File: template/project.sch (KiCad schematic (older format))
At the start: 1 part

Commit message: Continued play with libraries
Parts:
- added SW1: SW_Push, Buttons_Switches_SMD:SW_SPST_FSMSM, symbol SW_Push
- BT1: renamed from BT?; footprint (none) -> Battery_Holders:Keystone_103_1x20mm-CoinCell
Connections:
- net +3V3: now also SW1.1
- net Sheet59D70135/V_IN renamed reg/V_IN
- new net blue led/IN: SW1.2
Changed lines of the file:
@@
 $Descr A4 11693 8268
 encoding utf-8
-Sheet 1 3
+Sheet 1 5
 Title ""
 Date ""
@@
 S 4350 2800 500  150
 U 59D6FE5B
-F0 "Sheet59D6FE5A" 60
+F0 "green led" 60
 F1 "3v3/led/green.sch" 60
-F2 "3V3" I L 4350 2850 60
+F2 "IN" I L 4350 2850 60
 $EndSheet
 $Comp
-L Battery BT?
+L Battery BT1
 U 1 1 59D6FF4B
 P 3400 3950
-F 0 "BT?" H 3500 4050 50  0000 L CNN
+F 0 "BT1" H 3500 4050 50  0000 L CNN
 F 1 "Battery" H 3500 3950 50  0000 L CNN
-F 2 "" V 3400 4010 50  0001 C CNN
+F 2 "Battery_Holders:Keystone_103_1x20mm-CoinCell" V 3400 4010 50  0001 C CNN
 F 3 "" V 3400 4010 50  0001 C CNN
 	1    3400 3950
@@
 L GND #PWR01
 U 1 1 59D6FFA3
-P 3400 4150
-F 0 "#PWR01" H 3400 3900 50  0001 C CNN
-F 1 "GND" H 3400 4000 50  0000 C CNN
-F 2 "" H 3400 4150 50  0001 C CNN
-F 3 "" H 3400 4150 50  0001 C CNN
-	1    3400 4150
+P 3700 4350
+F 0 "#PWR01" H 3700 4100 50  0001 C CNN
+F 1 "GND" H 3700 4200 50  0000 C CNN
+F 2 "" H 3700 4350 50  0001 C CNN
+F 3 "" H 3700 4350 50  0001 C CNN
+	1    3700 4350
 	1    0    0    -1
 $EndComp
@@
 S 3900 3650 650  200
 U 59D70136
-F0 "Sheet59D70135" 60
+F0 "reg" 60
 F1 "3v3/reg.sch" 60
 F2 "V_IN" I L 3900 3750 60
@@
 Wire Wire Line
 	3400 3750 3900 3750
+Wire Wire Line
+	5100 3750 4550 3750
+Wire Wire Line
+	4000 2850 4350 2850
 $Comp
-L +3V3 #PWR02
+L PWR_FLAG #FLG02
+U 1 1 59D70465
+P 3450 3750
+F 0 "#FLG02" H 3450 3825 50  0001 C CNN
+F 1 "PWR_FLAG" H 3450 3900 50  0000 C CNN
+F 2 "" H 3450 3750 50  0001 C CNN
+F 3 "" H 3450 3750 50  0001 C CNN
+	1    3450 3750
+	1    0    0    -1
+$EndComp
+Connection ~ 3450 3750
+Wire Wire Line
+	3400 4350 3700 4350
+$Comp
+L PWR_FLAG #FLG03
+U 1 1 59D704F4
+P 3700 4350
+F 0 "#FLG03" H 3700 4425 50  0001 C CNN
+F 1 "PWR_FLAG" H 3700 4500 50  0000 C CNN
+F 2 "" H 3700 4350 50  0001 C CNN
+F 3 "" H 3700 4350 50  0001 C CNN
+	1    3700 4350
+	1    0    0    -1
+$EndComp
+Wire Wire Line
+	3400 4150 3400 4350
+$Sheet
+S 4450 2150 500  150
+U 59D70D6B
+F0 "blue led" 60
+F1 "3v3/led/blue.sch" 60
+F2 "IN" I L 4450 2200 60
+$EndSheet
+$Comp
+L SW_Push SW1
+U 1 1 59D70D94
+P 4150 2200
+F 0 "SW1" H 4200 2300 50  0000 L CNN
+F 1 "SW_Push" H 4150 2140 50  0000 C CNN
+F 2 "Buttons_Switches_SMD:SW_SPST_FSMSM" H 4150 2400 50  0001 C CNN
+F 3 "" H 4150 2400 50  0001 C CNN
+	1    4150 2200
+	1    0    0    -1
+$EndComp
+Wire Wire Line
+	4350 2200 4450 2200
+$Comp
+L +3V3 #PWR04
 U 1 1 59D7025D
 P 5100 3750
-F 0 "#PWR02" H 5100 3600 50  0001 C CNN
+F 0 "#PWR04" H 5100 3600 50  0001 C CNN
 F 1 "+3V3" H 5100 3890 50  0000 C CNN
 F 2 "" H 5100 3750 50  0001 C CNN
@@
 	1    0    0    -1
 $EndComp
-Wire Wire Line
-	5100 3750 4550 3750
 $Comp
-L +3V3 #PWR03
+L +3V3 #PWR05
 U 1 1 59D70291
 P 4000 2850
-F 0 "#PWR03" H 4000 2700 50  0001 C CNN
+F 0 "#PWR05" H 4000 2700 50  0001 C CNN
 F 1 "+3V3" H 4000 2990 50  0000 C CNN
 F 2 "" H 4000 2850 50  0001 C CNN
@@
 	1    0    0    -1
 $EndComp
+$Comp
+L +3V3 #PWR06
+U 1 1 59D70DD7
+P 3950 2200
+F 0 "#PWR06" H 3950 2050 50  0001 C CNN
+F 1 "+3V3" H 3950 2340 50  0000 C CNN
+F 2 "" H 3950 2200 50  0001 C CNN
+F 3 "" H 3950 2200 50  0001 C CNN
+	1    3950 2200
+	1    0    0    -1
+$EndComp
+$Sheet
+S 5700 2600 500  150
+U 59D71FBB
+F0 "red led" 60
+F1 "3v3/led/red.sch" 60
+F2 "IN" I L 5700 2650 60
+$EndSheet
 Wire Wire Line
-	4000 2850 4350 2850
+	4200 2850 4200 2600
 Wire Wire Line
-	4350 2850 4350 2850
+	4200 2600 5550 2600
+Wire Wire Line
+	5550 2600 5550 2650
+Wire Wire Line
+	5550 2650 5700 2650
+Connection ~ 4200 2850
 $EndSCHEMATC

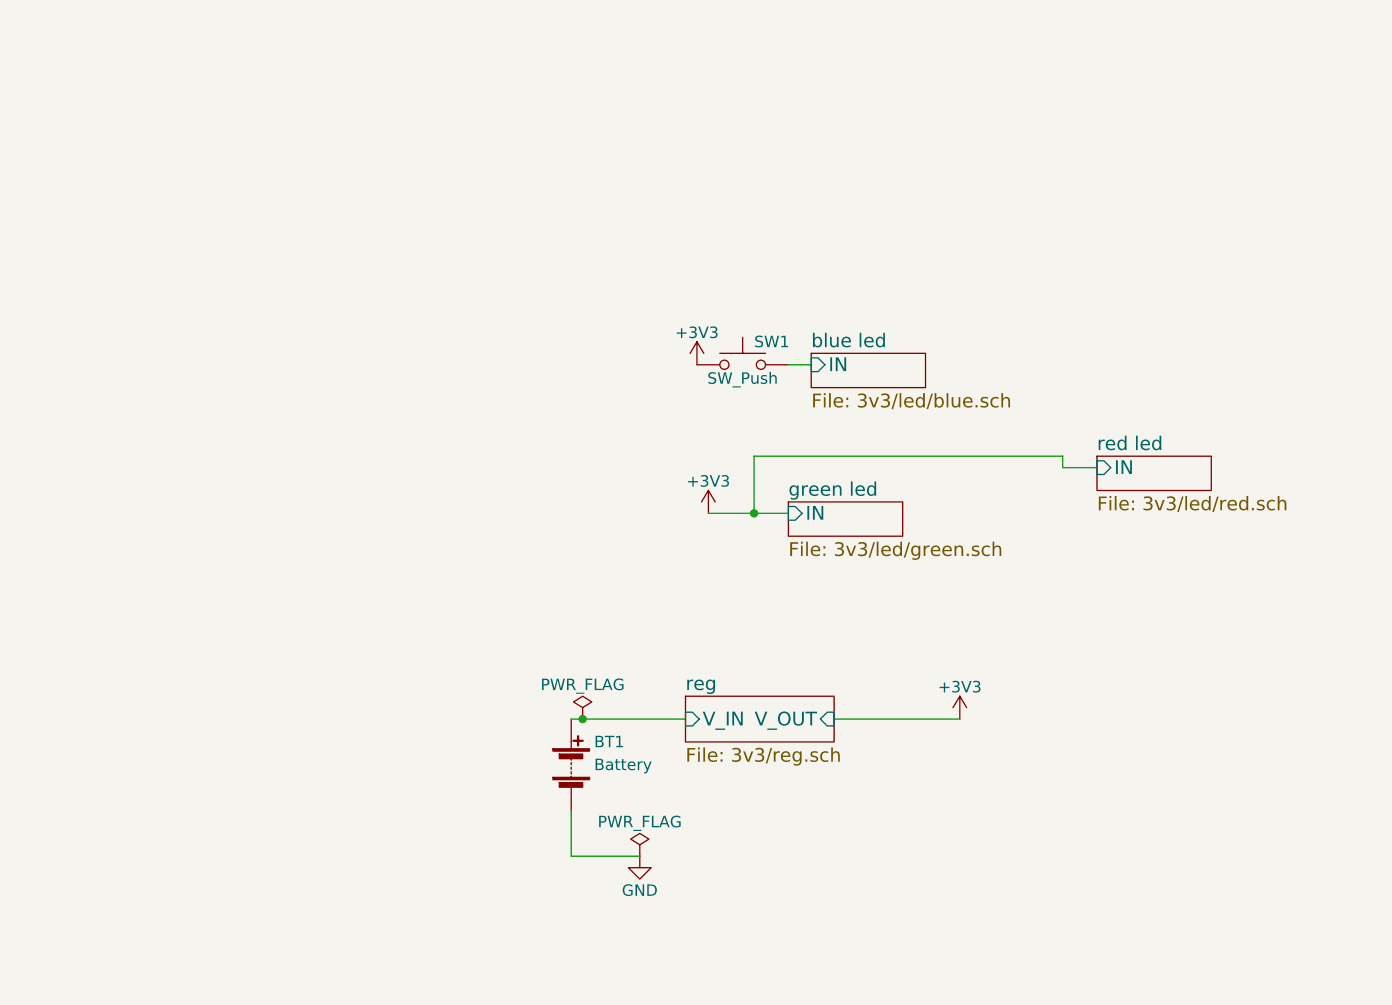
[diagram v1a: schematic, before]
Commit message: Added USB_UART connector
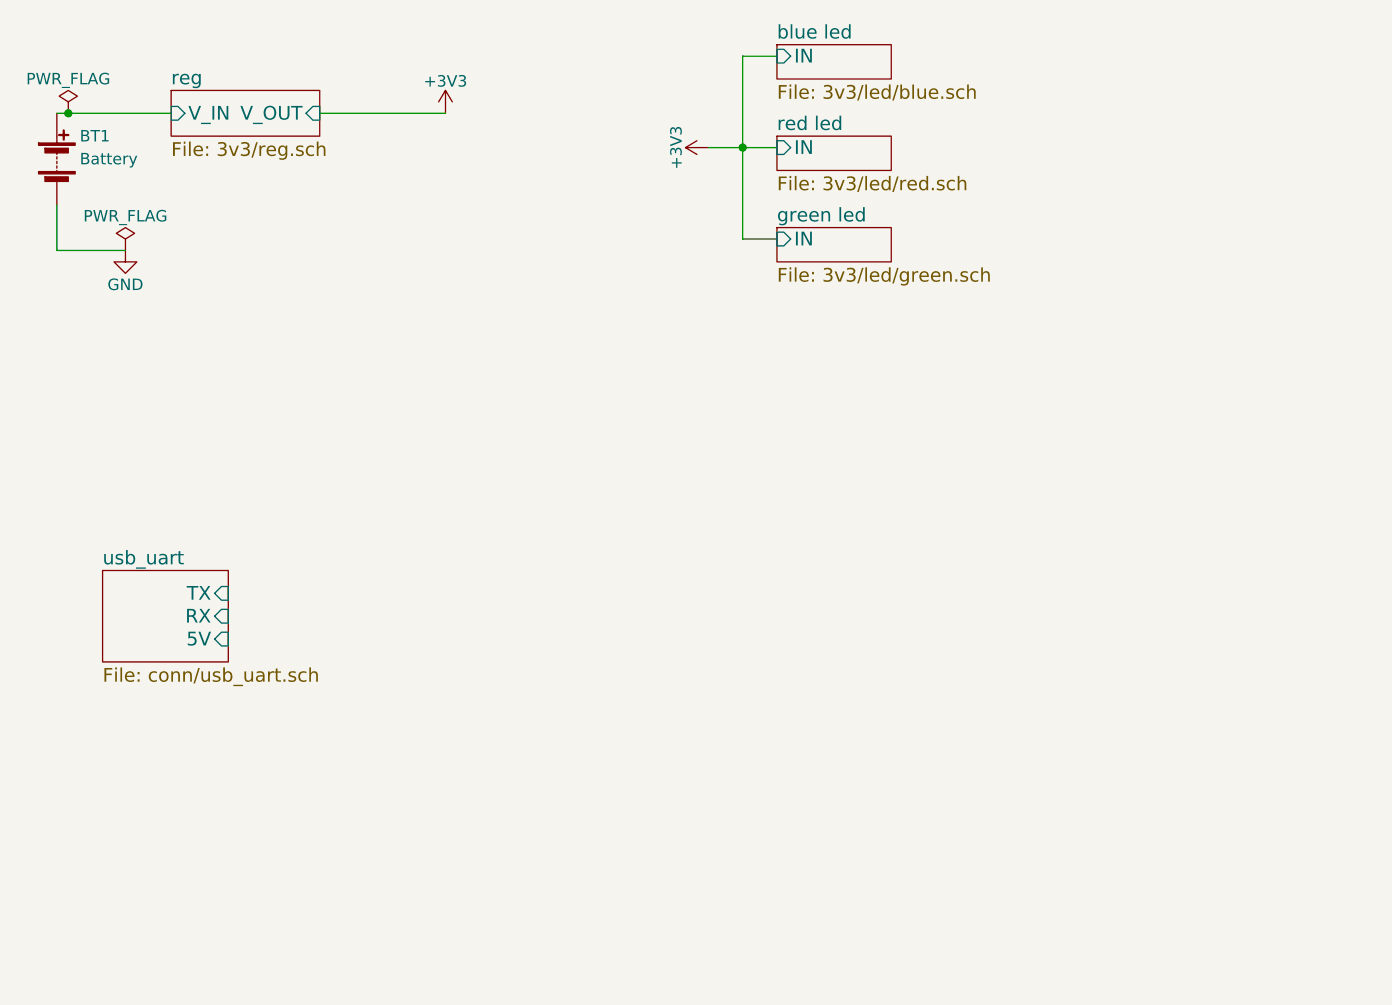
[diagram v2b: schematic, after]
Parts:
- removed SW1: SW_Push, Buttons_Switches_SMD:SW_SPST_FSMSM, symbol SW_Push
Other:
- moved on the sheet: BT1
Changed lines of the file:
@@
 EESchema Schematic File Version 2
+LIBS:ft230xs
+LIBS:usb_microb
 LIBS:power
 LIBS:device
@@
 LIBS:contrib
 LIBS:valves
+LIBS:project-cache
 EELAYER 25 0
 EELAYER END
 $Descr A4 11693 8268
 encoding utf-8
-Sheet 1 5
+Sheet 1 6
 Title ""
 Date ""
@@
 $EndDescr
 $Sheet
-S 4350 2800 500  150
+S 4300 1600 500  150
 U 59D6FE5B
 F0 "green led" 60
 F1 "3v3/led/green.sch" 60
-F2 "IN" I L 4350 2850 60
+F2 "IN" I L 4300 1650 60
 $EndSheet
 $Comp
 L Battery BT1
 U 1 1 59D6FF4B
-P 3400 3950
-F 0 "BT1" H 3500 4050 50  0000 L CNN
-F 1 "Battery" H 3500 3950 50  0000 L CNN
-F 2 "Battery_Holders:Keystone_103_1x20mm-CoinCell" V 3400 4010 50  0001 C CNN
-F 3 "" V 3400 4010 50  0001 C CNN
-	1    3400 3950
+P 1150 1300
+F 0 "BT1" H 1250 1400 50  0000 L CNN
+F 1 "Battery" H 1250 1300 50  0000 L CNN
+F 2 "Battery_Holders:Keystone_103_1x20mm-CoinCell" V 1150 1360 50  0001 C CNN
+F 3 "" V 1150 1360 50  0001 C CNN
+	1    1150 1300
 	1    0    0    -1
 $EndComp
@@
 L GND #PWR01
 U 1 1 59D6FFA3
-P 3700 4350
-F 0 "#PWR01" H 3700 4100 50  0001 C CNN
-F 1 "GND" H 3700 4200 50  0000 C CNN
-F 2 "" H 3700 4350 50  0001 C CNN
-F 3 "" H 3700 4350 50  0001 C CNN
-	1    3700 4350
+P 1450 1700
+F 0 "#PWR01" H 1450 1450 50  0001 C CNN
+F 1 "GND" H 1450 1550 50  0000 C CNN
+F 2 "" H 1450 1700 50  0001 C CNN
+F 3 "" H 1450 1700 50  0001 C CNN
+	1    1450 1700
 	1    0    0    -1
 $EndComp
 $Sheet
-S 3900 3650 650  200
+S 1650 1000 650  200
 U 59D70136
 F0 "reg" 60
 F1 "3v3/reg.sch" 60
-F2 "V_IN" I L 3900 3750 60
-F3 "V_OUT" I R 4550 3750 60
+F2 "V_IN" I L 1650 1100 60
+F3 "V_OUT" I R 2300 1100 60
 $EndSheet
 Wire Wire Line
-	3400 3750 3900 3750
+	1150 1100 1650 1100
 Wire Wire Line
-	5100 3750 4550 3750
-Wire Wire Line
-	4000 2850 4350 2850
+	2850 1100 2300 1100
 $Comp
 L PWR_FLAG #FLG02
 U 1 1 59D70465
-P 3450 3750
-F 0 "#FLG02" H 3450 3825 50  0001 C CNN
-F 1 "PWR_FLAG" H 3450 3900 50  0000 C CNN
-F 2 "" H 3450 3750 50  0001 C CNN
-F 3 "" H 3450 3750 50  0001 C CNN
-	1    3450 3750
+P 1200 1100
+F 0 "#FLG02" H 1200 1175 50  0001 C CNN
+F 1 "PWR_FLAG" H 1200 1250 50  0000 C CNN
+F 2 "" H 1200 1100 50  0001 C CNN
+F 3 "" H 1200 1100 50  0001 C CNN
+	1    1200 1100
 	1    0    0    -1
 $EndComp
-Connection ~ 3450 3750
+Connection ~ 1200 1100
 Wire Wire Line
-	3400 4350 3700 4350
+	1150 1700 1450 1700
 $Comp
 L PWR_FLAG #FLG03
 U 1 1 59D704F4
-P 3700 4350
-F 0 "#FLG03" H 3700 4425 50  0001 C CNN
-F 1 "PWR_FLAG" H 3700 4500 50  0000 C CNN
-F 2 "" H 3700 4350 50  0001 C CNN
-F 3 "" H 3700 4350 50  0001 C CNN
-	1    3700 4350
+P 1450 1700
+F 0 "#FLG03" H 1450 1775 50  0001 C CNN
+F 1 "PWR_FLAG" H 1450 1850 50  0000 C CNN
+F 2 "" H 1450 1700 50  0001 C CNN
+F 3 "" H 1450 1700 50  0001 C CNN
+	1    1450 1700
 	1    0    0    -1
 $EndComp
 Wire Wire Line
-	3400 4150 3400 4350
+	1150 1500 1150 1700
 $Sheet
-S 4450 2150 500  150
+S 4300 800  500  150
 U 59D70D6B
 F0 "blue led" 60
 F1 "3v3/led/blue.sch" 60
-F2 "IN" I L 4450 2200 60
+F2 "IN" I L 4300 850 60
 $EndSheet
-$Comp
-L SW_Push SW1
-U 1 1 59D70D94
-P 4150 2200
-F 0 "SW1" H 4200 2300 50  0000 L CNN
-F 1 "SW_Push" H 4150 2140 50  0000 C CNN
-F 2 "Buttons_Switches_SMD:SW_SPST_FSMSM" H 4150 2400 50  0001 C CNN
-F 3 "" H 4150 2400 50  0001 C CNN
-	1    4150 2200
-	1    0    0    -1
-$EndComp
-Wire Wire Line
-	4350 2200 4450 2200
 $Comp
 L +3V3 #PWR04
 U 1 1 59D7025D
-P 5100 3750
-F 0 "#PWR04" H 5100 3600 50  0001 C CNN
-F 1 "+3V3" H 5100 3890 50  0000 C CNN
-F 2 "" H 5100 3750 50  0001 C CNN
-F 3 "" H 5100 3750 50  0001 C CNN
-	1    5100 3750
+P 2850 1100
+F 0 "#PWR04" H 2850 950 50  0001 C CNN
+F 1 "+3V3" H 2850 1240 50  0000 C CNN
+F 2 "" H 2850 1100 50  0001 C CNN
+F 3 "" H 2850 1100 50  0001 C CNN
+	1    2850 1100
 	1    0    0    -1
 $EndComp
 $Comp
 L +3V3 #PWR05
-U 1 1 59D70291
-P 4000 2850
-F 0 "#PWR05" H 4000 2700 50  0001 C CNN
-F 1 "+3V3" H 4000 2990 50  0000 C CNN
-F 2 "" H 4000 2850 50  0001 C CNN
-F 3 "" H 4000 2850 50  0001 C CNN
-	1    4000 2850
-	1    0    0    -1
-$EndComp
-$Comp
-L +3V3 #PWR06
 U 1 1 59D70DD7
-P 3950 2200
-F 0 "#PWR06" H 3950 2050 50  0001 C CNN
-F 1 "+3V3" H 3950 2340 50  0000 C CNN
-F 2 "" H 3950 2200 50  0001 C CNN
-F 3 "" H 3950 2200 50  0001 C CNN
-	1    3950 2200
-	1    0    0    -1
+P 4000 1250
+F 0 "#PWR05" H 4000 1100 50  0001 C CNN
+F 1 "+3V3" H 4000 1390 50  0000 C CNN
+F 2 "" H 4000 1250 50  0001 C CNN
+F 3 "" H 4000 1250 50  0001 C CNN
+	1    4000 1250
+	0    -1   -1   0
 $EndComp
 $Sheet
-S 5700 2600 500  150
+S 4300 1200 500  150
 U 59D71FBB
 F0 "red led" 60
 F1 "3v3/led/red.sch" 60
-F2 "IN" I L 5700 2650 60
+F2 "IN" I L 4300 1250 60
 $EndSheet
 Wire Wire Line
-	4200 2850 4200 2600
+	4000 1250 4300 1250
 Wire Wire Line
-	4200 2600 5550 2600
+	4150 850  4150 1650
 Wire Wire Line
-	5550 2600 5550 2650
+	4150 850  4300 850
+Connection ~ 4150 1250
 Wire Wire Line
-	5550 2650 5700 2650
-Connection ~ 4200 2850
+	4150 1650 4300 1650
+$Sheet
+S 1350 3100 550  400
+U 59D74113
+F0 "usb_uart" 60
+F1 "conn/usb_uart.sch" 60
+F2 "TX" I R 1900 3200 60
+F3 "RX" I R 1900 3300 60
+F4 "5V" I R 1900 3400 60
+$EndSheet
 $EndSCHEMATC

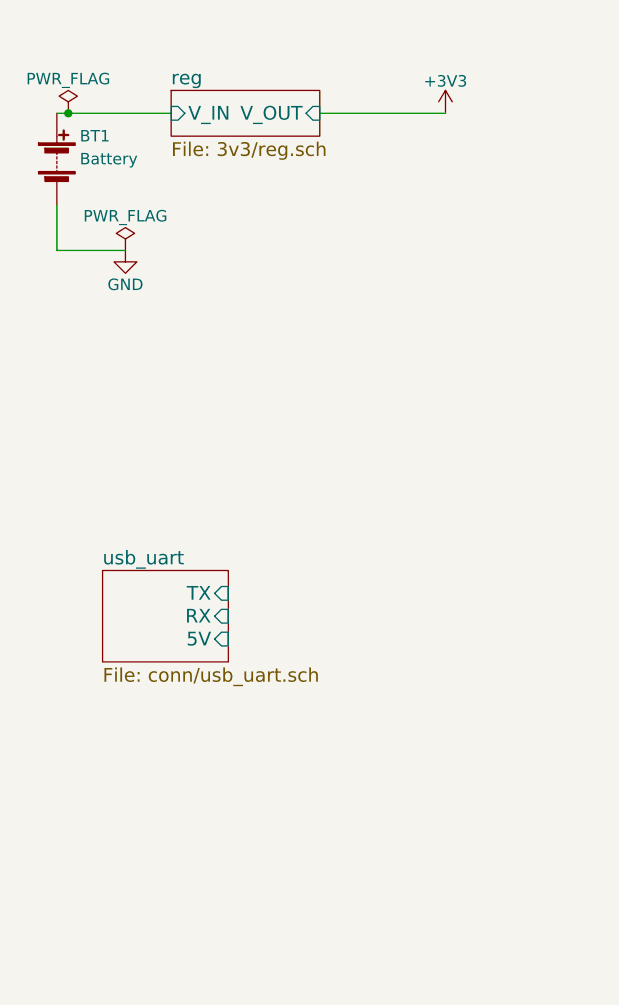
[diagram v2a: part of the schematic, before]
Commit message: Fixed micro SD card
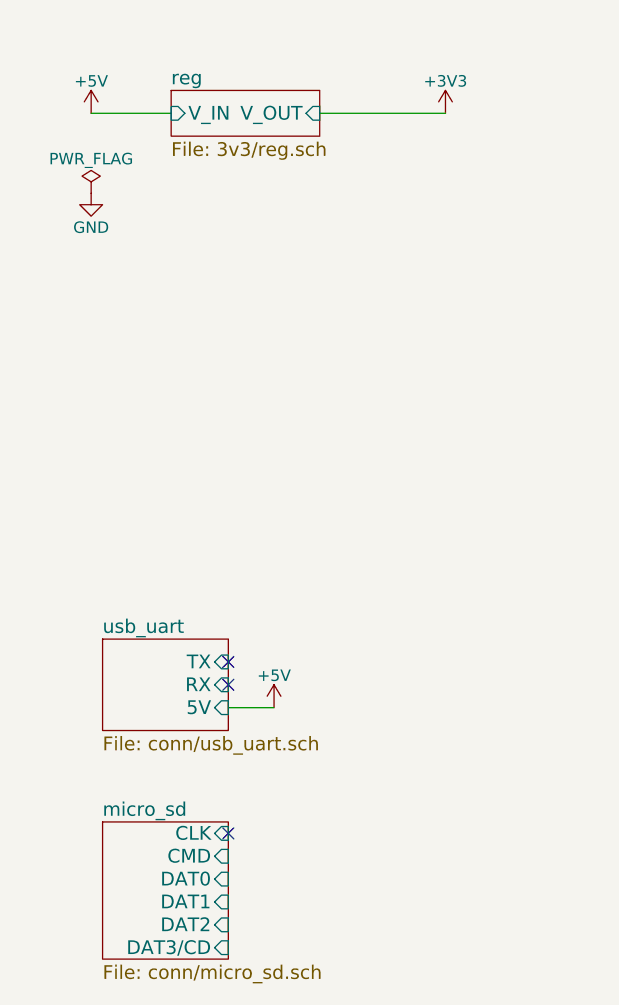
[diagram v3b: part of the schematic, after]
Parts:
- removed BT1: Battery, Battery_Holders:Keystone_103_1x20mm-CoinCell, symbol Battery
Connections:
- no-connect marks 0 -> 3
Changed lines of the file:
@@
 LIBS:ft230xs
 LIBS:usb_microb
+LIBS:micro_sd_card
 LIBS:power
 LIBS:device
@@
 $Descr A4 11693 8268
 encoding utf-8
-Sheet 1 6
+Sheet 1 7
 Title ""
 Date ""
@@
 $EndSheet
 $Comp
-L Battery BT1
-U 1 1 59D6FF4B
-P 1150 1300
-F 0 "BT1" H 1250 1400 50  0000 L CNN
-F 1 "Battery" H 1250 1300 50  0000 L CNN
-F 2 "Battery_Holders:Keystone_103_1x20mm-CoinCell" V 1150 1360 50  0001 C CNN
-F 3 "" V 1150 1360 50  0001 C CNN
-	1    1150 1300
-	1    0    0    -1
-$EndComp
-$Comp
 L GND #PWR01
 U 1 1 59D6FFA3
-P 1450 1700
-F 0 "#PWR01" H 1450 1450 50  0001 C CNN
-F 1 "GND" H 1450 1550 50  0000 C CNN
-F 2 "" H 1450 1700 50  0001 C CNN
-F 3 "" H 1450 1700 50  0001 C CNN
-	1    1450 1700
+P 1300 1450
+F 0 "#PWR01" H 1300 1200 50  0001 C CNN
+F 1 "GND" H 1300 1300 50  0000 C CNN
+F 2 "" H 1300 1450 50  0001 C CNN
+F 3 "" H 1300 1450 50  0001 C CNN
+	1    1300 1450
 	1    0    0    -1
 $EndComp
@@
 $EndSheet
 Wire Wire Line
-	1150 1100 1650 1100
-Wire Wire Line
 	2850 1100 2300 1100
 $Comp
 L PWR_FLAG #FLG02
-U 1 1 59D70465
-P 1200 1100
-F 0 "#FLG02" H 1200 1175 50  0001 C CNN
-F 1 "PWR_FLAG" H 1200 1250 50  0000 C CNN
-F 2 "" H 1200 1100 50  0001 C CNN
-F 3 "" H 1200 1100 50  0001 C CNN
-	1    1200 1100
+U 1 1 59D704F4
+P 1300 1450
+F 0 "#FLG02" H 1300 1525 50  0001 C CNN
+F 1 "PWR_FLAG" H 1300 1600 50  0000 C CNN
+F 2 "" H 1300 1450 50  0001 C CNN
+F 3 "" H 1300 1450 50  0001 C CNN
+	1    1300 1450
 	1    0    0    -1
 $EndComp
-Connection ~ 1200 1100
-Wire Wire Line
-	1150 1700 1450 1700
-$Comp
-L PWR_FLAG #FLG03
-U 1 1 59D704F4
-P 1450 1700
-F 0 "#FLG03" H 1450 1775 50  0001 C CNN
-F 1 "PWR_FLAG" H 1450 1850 50  0000 C CNN
-F 2 "" H 1450 1700 50  0001 C CNN
-F 3 "" H 1450 1700 50  0001 C CNN
-	1    1450 1700
-	1    0    0    -1
-$EndComp
-Wire Wire Line
-	1150 1500 1150 1700
 $Sheet
 S 4300 800  500  150
@@
 $EndSheet
 $Comp
-L +3V3 #PWR04
+L +3V3 #PWR03
 U 1 1 59D7025D
 P 2850 1100
-F 0 "#PWR04" H 2850 950 50  0001 C CNN
+F 0 "#PWR03" H 2850 950 50  0001 C CNN
 F 1 "+3V3" H 2850 1240 50  0000 C CNN
 F 2 "" H 2850 1100 50  0001 C CNN
@@
 $EndComp
 $Comp
-L +3V3 #PWR05
+L +3V3 #PWR04
 U 1 1 59D70DD7
 P 4000 1250
-F 0 "#PWR05" H 4000 1100 50  0001 C CNN
+F 0 "#PWR04" H 4000 1100 50  0001 C CNN
 F 1 "+3V3" H 4000 1390 50  0000 C CNN
 F 2 "" H 4000 1250 50  0001 C CNN
@@
 	4150 1650 4300 1650
 $Sheet
-S 1350 3100 550  400
+S 1350 3400 550  400
 U 59D74113
 F0 "usb_uart" 60
 F1 "conn/usb_uart.sch" 60
-F2 "TX" I R 1900 3200 60
-F3 "RX" I R 1900 3300 60
-F4 "5V" I R 1900 3400 60
+F2 "TX" I R 1900 3500 60
+F3 "RX" I R 1900 3600 60
+F4 "5V" I R 1900 3700 60
 $EndSheet
+$Comp
+L +5V #PWR05
+U 1 1 59D72A34
+P 2100 3700
+F 0 "#PWR05" H 2100 3550 50  0001 C CNN
+F 1 "+5V" H 2100 3840 50  0000 C CNN
+F 2 "" H 2100 3700 50  0001 C CNN
+F 3 "" H 2100 3700 50  0001 C CNN
+	1    2100 3700
+	1    0    0    -1
+$EndComp
+Wire Wire Line
+	2100 3700 1900 3700
+$Comp
+L +5V #PWR06
+U 1 1 59D72C7E
+P 1300 1100
+F 0 "#PWR06" H 1300 950 50  0001 C CNN
+F 1 "+5V" H 1300 1240 50  0000 C CNN
+F 2 "" H 1300 1100 50  0001 C CNN
+F 3 "" H 1300 1100 50  0001 C CNN
+	1    1300 1100
+	1    0    0    -1
+$EndComp
+Wire Wire Line
+	1300 1100 1650 1100
+$Sheet
+S 1350 4200 550  600
+U 59D73210
+F0 "micro_sd" 60
+F1 "conn/micro_sd.sch" 60
+F2 "CLK" I R 1900 4250 60
+F3 "CMD" I R 1900 4350 60
+F4 "DAT0" I R 1900 4450 60
+F5 "DAT1" I R 1900 4550 60
+F6 "DAT2" I R 1900 4650 60
+F7 "DAT3/CD" I R 1900 4750 60
+$EndSheet
+NoConn ~ 1900 3500
+NoConn ~ 1900 3600
+NoConn ~ 1900 4250
 $EndSCHEMATC
